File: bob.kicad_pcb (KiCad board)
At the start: 2 copper layers, 58.4 x 25.4 mm, 52 parts, among them J1 Mini USB Female, J2 GPIO (Optional), J3 GPIO (Optional), J4 Screw Terminal, 2.54mm, J5 Conn_01x04_Male, J6 Conn_01x03_Male, Q1 IRFML8244TRPBF, Q2 IRFML8244TRPBF, U1 W25Q64JVSS, U2 AMS1117-3.3, U3 RP2040, U4 QMI8658C, U5 HP203B, U6 QMC5883L, Y1 12MHz

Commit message: Rev 4 issued for production
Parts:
- removed JP1: BOOTSEL, Button_Switch_SMD:SW_SPST_B3U-1000P
- removed TP1, TP2: TestPoint, TestPoint:TestPoint_Pad_D1.0mm
- removed the YAR at (23.4, 30.5)
- added BZ1: Buzzer, YAR_other:Cy-SMD-4020-3040, F.Cu at (50.4, 23.4)
- added C15: 220n, Capacitor_SMD:C_0603_1608Metric, B.Cu at (31.0, 35.1)
- added C16: 100n, Capacitor_SMD:C_0603_1608Metric, B.Cu at (31.0, 36.6)
- added C17: 10u, Capacitor_SMD:C_0603_1608Metric, B.Cu at (26.2, 20.6)
- added C18: 10u, Capacitor_SMD:C_0603_1608Metric, B.Cu at (26.2, 22.1)
- added D6: B5819W SL, Diode_SMD:D_SOD-123, F.Cu at (63.2, 30.0)
- added D7: B5819W SL, Diode_SMD:D_SOD-123, F.Cu at (63.1, 37.8)
- added Q3: AO3400A, Package_TO_SOT_SMD:SOT-23, F.Cu at (63.1, 34.5)
- added R10: 220, Resistor_SMD:R_0603_1608Metric, B.Cu at (37.1, 25.7)
- added R11: 220, Resistor_SMD:R_0603_1608Metric, B.Cu at (37.1, 27.2)
- added R12: 1k, Resistor_SMD:R_0603_1608Metric, B.Cu at (26.2, 41.7)
- added R8: 3k6, Resistor_SMD:R_0603_1608Metric, B.Cu at (46.2, 35.1)
- added R9: 3k6, Resistor_SMD:R_0603_1608Metric, B.Cu at (46.2, 36.6)
- added SW1: Bootsel, Button_Switch_SMD:SW_SPST_TL3342, F.Cu at (23.4, 35.6)
- added U7: W25Q128JVSS, Package_SO:SOIC-8_5.23x5.23mm_P1.27mm, F.Cu at (57.4, 25.7)
- added YAR: LOGO, YAR_Logos:yar_new, B.Cu at (24.1, 27.9)
- C1: value 100n -> 7p; footprint Capacitor_SMD:C_0603_1608Metric -> Capacitor_SMD:C_0402_1005Metric
- C10, C11, C5: moved to B.Cu
- C12: value 4.7u -> 100n; moved to B.Cu
- C13: value 220n -> 100n; moved to B.Cu
- C14: value 100n -> 4.7u; moved to B.Cu
- C2: value 10u -> 7p; footprint Capacitor_SMD:C_0603_1608Metric -> Capacitor_SMD:C_0402_1005Metric
- C3: value 10u -> 100n; moved to B.Cu
- C4, C6: value 1u -> 100n; moved to B.Cu
- C7: value 100n -> 1u; moved to B.Cu
- C8: value 4p -> 1u; moved to B.Cu
- C9: value 4p -> 100n; moved to B.Cu
- D1, D2, D5: value 1N4007 -> B5819W SL
- D3: value RED -> GREEN
- D4: value 1N4007 -> RED; footprint Diode_SMD:D_SOD-123 -> LED_SMD:LED_0603_1608Metric
- J1: value Mini USB Female -> Micro USB Female; footprint Connector_USB:USB_Mini-B_Lumberg_2486_01_Horizontal -> Connector_USB:USB_Micro-B_Molex-105017-0001
- J2: value GPIO (Optional) -> Screw Terminal, 2.54mm; footprint Connector_PinHeader_2.54mm:PinHeader_1x07_P2.54mm_Vertical_NoSilk -> YAR_Connectors:ScrewTerm_2.54x02
- J3: footprint Connector_PinHeader_2.54mm:PinHeader_1x07_P2.54mm_Vertical_NoSilk -> Connector_PinHeader_2.54mm:PinHeader_1x11_P2.54mm_Vertical
- J4: value Screw Terminal, 2.54mm -> GPIO (Optional); footprint YAR_Connectors:ScrewTerm_2.54x06 -> Connector_PinHeader_2.54mm:PinHeader_1x11_P2.54mm_Vertical
- J5: value Conn_01x04_Male -> Conn_01x03_Male; footprint YAR_Connectors:ScrewTerm_2.54x04 -> Connector_PinHeader_2.54mm:PinHeader_1x03_P2.54mm_Vertical
- J6: value Conn_01x03_Male -> Conn_01x06_Pin; footprint Connector_PinHeader_2.54mm:PinHeader_1x02_P2.54mm_Vertical -> YAR_Connectors:ScrewTerm_2.54x06; moved to F.Cu
- Q1, Q2: value IRFML8244TRPBF -> AO3400A
- R1: value 220 -> 27; footprint Resistor_SMD:R_0603_1608Metric -> Resistor_SMD:R_0603_1608Metric_Pad0.98x0.95mm_HandSolder
- R3: value 27 -> 1k; footprint Resistor_SMD:R_0603_1608Metric_Pad0.98x0.95mm_HandSolder -> Resistor_SMD:R_0603_1608Metric
- R4, R5: value 1k -> 3k6
- R6, R7: value 10k -> 4; footprint Resistor_SMD:R_0603_1608Metric -> Resistor_SMD:R_0805_2012Metric; moved to B.Cu
- RN1, RN2: value 22k -> 10k; moved to B.Cu
- U1: value W25Q64JVSS -> AMS1117-3.3; footprint Package_SO:SOIC-8_5.23x5.23mm_P1.27mm -> Package_TO_SOT_SMD:SOT-223-3_TabPin2
- U2: value AMS1117-3.3 -> W25Q128JVSS; footprint Package_TO_SOT_SMD:SOT-223-3_TabPin2 -> Package_SO:SOIC-8_5.23x5.23mm_P1.27mm
- U3: value RP2040 -> QMC5883L; footprint YAR_MCU:RP2040-QFN-56_HS -> YAR_Sensors:QMC5883L-LGA16
- U4: value QMI8658C -> HP203B; footprint YAR_Sensors:QMI8658C-LGA14 -> YAR_Sensors:HP203B-LGA8
- U5: value HP203B -> RP2040; footprint YAR_Sensors:HP203B-LGA8 -> YAR_MCU:RP2040-QFN-56
- U6: value QMC5883L -> QMI8658C; footprint YAR_Sensors:QMC5883L-LGA16 -> YAR_Sensors:QMI8658C-LGA14
- Y1: footprint Crystal:Crystal_SMD_5032-2Pin_5.0x3.2mm -> Crystal:Crystal_SMD_3225-4Pin_3.2x2.5mm
- moved C14 37.7 mm to (31.0, 33.5), turned to 0 degrees
- moved R4 37.6 mm to (66.0, 19.1)
- moved J4 36.2 mm to (30.5, 41.9), turned to 90 degrees
- moved C2 34.8 mm to (54.8, 37.8), turned to 90 degrees
- moved C13 32.2 mm to (37.1, 33.3)
- moved C12 30.7 mm to (40.1, 36.6)
- moved C1 30.6 mm to (49.6, 37.6), turned to -90 degrees
- moved J6 29.5 mm to (69.1, 30.5), turned to 90 degrees
- moved U6 25.3 mm to (43.0, 38.1), turned to -90 degrees
- moved J2 24.7 mm to (17.1, 35.6)
- moved J3 23.4 mm to (30.5, 19.1)
- moved C11 22.9 mm to (40.1, 33.3)
- moved D5 22.4 mm to (60.5, 19.3)
- moved C3 21.9 mm to (56.2, 25.7)
- moved R5 19.3 mm to (66.0, 20.6)
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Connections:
- C1 pad 1: +3V3 -> GND
- C1 pad 2: GND -> Net-(U5-XIN)
- C12 pad 1: GND -> +3V3
- C12 pad 2: Net-(C17-Pad2) -> GND
- C13 pad 1: Net-(C18-Pad1) -> +3V3
- C13 pad 2: Net-(C18-Pad2) -> GND
- C14 pad 1: +3V3 -> GND
- C14 pad 2: GND -> Net-(U3-C1)
- C2 pad 1: Net-(C10-Pad1) -> GND
- C2 pad 2: GND -> Net-(C2-Pad2)
- C8 pad 1: GND -> +1V1
- C8 pad 2: Net-(C13-Pad2) -> GND
- C9 pad 1: GND -> +3V3
- C9 pad 2: XIN -> GND
- D1 pad 1: Net-(C10-Pad1) -> Net-(D1-K)
- D2 pad 1: Net-(C10-Pad1) -> Net-(D1-K)
- D3 pad 1: Net-(D1-Pad1) -> Net-(D3-K)
- D3 pad 2: Net-(D1-Pad2) -> Net-(D3-A)
- D4 pad 1: +3V3 -> Net-(D4-K)
- D4 pad 2: Cont 2 -> +3V3
- D5 pad 2: Cont 1 -> Net-(D5-A)
- F1 pad 1: Net-(F1-Pad1) -> Net-(J6-Pin_5)
- J2 pad 1: VBUS -> GND
- J3 pad 1: +3V3 -> VBUS
- J3 pad 2: GPIO0 -> +BATT
- J3 pad 3: GPIO1 -> GPIO29
- J3 pad 4: GPIO2 -> GPIO28
- J3 pad 5: GPIO3 -> GPIO27
- J3 pad 6: GPIO4 -> GPIO26
- J3 pad 7: GND -> GPIO24
- J4 pad 1: GND -> +3V3
- J4 pad 2: Net-(J2-Pad2) -> GPIO0
- J4 pad 3: Net-(J2-Pad2) -> GPIO1
- J4 pad 4: +BATT -> GPIO2
- J4 pad 5: +BATT -> GPIO3
- J4 pad 6: Net-(F1-Pad1) -> GPIO4
- J5 pad 1: Fire 1 -> GND
- J5 pad 2: ARM -> SWD
- J5 pad 3: Fire 2 -> SWCLK
- J6 pad 1: SWD -> GND
- J6 pad 2: SWCLK -> Cont 2
- Q1 pad 1: Pyro 1 -> BUZZER
- Q1 pad 2: Fire 1 -> GND
- Q1 pad 3: GND -> Net-(BZ1-+)
- Q2 pad 1: Pyro 2 -> Pyro 1
- Q2 pad 2: Fire 2 -> Cont 1
- Q2 pad 3: GND -> Net-(Q2-D)
- R1 pad 1: Net-(D1-Pad1) -> Net-(U5-USB_DM)
- R1 pad 2: GND -> USB_D-
- R2 pad 1: Net-(R2-Pad1) -> Net-(U5-USB_DP)
- R2 pad 2: USB_D- -> USB_D+
- R3 pad 1: Net-(R1-Pad1) -> Net-(C2-Pad2)
- R3 pad 2: USB_D+ -> Net-(U5-XOUT)
- R4 pad 1: Net-(JP1-Pad2) -> ARMED
- R4 pad 2: QSPI_SS -> Net-(D5-A)
- R5 pad 1: Net-(C13-Pad2) -> Net-(D5-A)
- R5 pad 2: XOUT -> ARM
- R6 pad 1: I2C_SCL -> ARM
- R6 pad 2: +3V3 -> Net-(Q2-D)
- R7 pad 1: I2C_SDA -> ARM
- R7 pad 2: +3V3 -> Net-(Q3-D)
- RN1 pad 1: Pyro 2 -> GND
- RN1 pad 2: Fire 2 -> Cont 1
- RN1 pad 3: Cont 2 -> Net-(RN1C-R3.1)
- RN1 pad 4: Net-(RN2-Pad4) -> GND
- RN1 pad 5: GND -> Net-(RN1C-R3.1)
- RN1 pad 6: Net-(RN2-Pad4) -> Cont 1
- RN1 pad 7: Cont 2 -> ARM
- RN1 pad 8: GND -> Pyro 1
- RN2 pad 1: Pyro 1 -> GND
- RN2 pad 2: Fire 1 -> Cont 2
- RN2 pad 3: Cont 1 -> Net-(RN2C-R3.1)
- RN2 pad 4: Net-(RN1-Pad4) -> GND
- RN2 pad 5: GND -> Net-(RN2C-R3.1)
- RN2 pad 6: Net-(RN1-Pad4) -> Cont 2
- RN2 pad 7: Cont 1 -> ARM
- RN2 pad 8: GND -> Pyro 2
- U1 pad 1: QSPI_SS -> GND
- U1 pad 2: QSPI_SD1 -> +3V3
- U1 pad 3: QSPI_SD2 -> Net-(D1-K)
- U2 pad 1: GND -> QSPI_SS
- U2 pad 2: +3V3 -> QSPI_SD1
- U2 pad 3: Net-(C10-Pad1) -> QSPI_SD2
- U3 pad 1: +3V3 -> I2C_SCL
- U3 pad 10: +3V3 -> Net-(U3-C1)
- U3 pad 11: Pyro 2 -> GND
- U3 pad 12: unconnected-(U1-Pad12) -> Net-(U3-SETC)
- U3 pad 13: QMI_INT2 -> +3V3
- U3 pad 14: QMI_INT1 -> (no net)
- U3 pad 15: I2C_SDA -> QMC_DRDY
- U3 pad 16: I2C_SCL -> I2C_SDA
- U3 pad 2: GPIO0 -> +3V3
- U3 pad 3: GPIO1 -> (no net)
- U3 pad 4: GPIO2 -> +3V3
- U3 pad 5: GPIO3 -> (no net)
- U3 pad 6: GPIO4 -> (no net)
- U3 pad 7: Cont 1 -> (no net)
- U3 pad 8: Cont 2 -> Net-(U3-SETP)
- U3 pad 9: Pyro 1 -> GND
- U4 pad 1: GND -> unconnected-(U4-INT1-Pad1)
- U4 pad 3: GND -> +3V3
- U4 pad 4: QMI_INT1 -> (no net)
- U4 pad 5: (no net) -> I2C_SCL
- U4 pad 6: GND -> I2C_SDA
- U4 pad 7: GND -> unconnected-(U4-INT0-Pad7)
- U5 pad 1: unconnected-(U5-Pad1) -> +3V3
- U5 pad 2: GND -> GPIO0
- U5 pad 3: +3V3 -> GPIO1
- U5 pad 4: (no net) -> GPIO2
- U5 pad 5: I2C_SCL -> GPIO3
- U5 pad 6: I2C_SDA -> GPIO4
- U5 pad 7: unconnected-(U5-Pad7) -> GPIO5
- U5 pad 8: +3V3 -> GPIO6
- U6 pad 1: I2C_SCL -> GND
- U6 pad 10: Net-(C17-Pad2) -> (no net)
- U6 pad 11: GND -> (no net)
- U6 pad 12: Net-(C18-Pad2) -> +3V3
- U6 pad 13: +3V3 -> I2C_SCL
- U6 pad 14: (no net) -> I2C_SDA
- U6 pad 2: +3V3 -> GND
- U6 pad 3: (no net) -> GND
- U6 pad 4: +3V3 -> QMI_INT1
- U6 pad 6: (no net) -> GND
- U6 pad 7: (no net) -> GND
- U6 pad 8: Net-(C18-Pad1) -> +3V3
- U6 pad 9: GND -> QMI_INT2
- Y1 pad 1: Net-(C13-Pad2) -> Net-(C2-Pad2)
- Y1 pad 2: XIN -> GND
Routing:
- net +3V3: track 117.1 -> 18.4 mm, vias 10 -> 27
- net ARMED: track 0.00 -> 26.2 mm, vias 0 -> 1
- net Cont 1: track 15.3 -> 39.2 mm, vias 0 -> 3
- net Cont 2: track 12.4 -> 35.9 mm, vias 0 -> 3
- net +BATT: track 48.9 -> 70.9 mm, vias 1 -> 2
- net +1V1: track 20.7 -> 2.02 mm, vias 0 -> 2
- net GPIO6: track 0.00 -> 15.7 mm
- net Net-(F1-Pad1): track 15.0 -> 0.00 mm, vias 1 -> 0
- net SPI_TX: track 0.00 -> 14.5 mm, vias 0 -> 2
- net Fire 2: track 14.1 -> 0.00 mm
- net GPIO5: track 0.00 -> 14.0 mm
- net SPI_SCLK: track 0.00 -> 13.7 mm, vias 0 -> 2
- net SWCLK: track 5.67 -> 19.1 mm
- net SWD: track 7.31 -> 20.6 mm
- net XIN: track 11.6 -> 0.00 mm
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- added copper zone on F.Cu, net +1V1
- added copper zone on In1.Cu, net +3V3
- added copper zone on In2.Cu, net GND
- removed copper zone on F.Cu, net +BATT
- removed copper zone on F.Cu, net Net-(C10-Pad1)
- removed copper zone on B.Cu, net Net-(J2-Pad2)
- removed copper zone on F.Cu, net Net-(J2-Pad2)
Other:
- copper layers 2 -> 4
- board text added: "00"
- board text added: "01"
- board text added: "02"
- board text added: "03"
- board text added: "04"
- board text added: "05"
- board text added: "06"
- board text added: "12V MAX"
- board text added: "22"
- board text added: "23"
- board text added: "24"
- board text added: "3v3"
- board text added: "ARMED"
- board text added: "Bob Rev 4A Claire H 2023"
- board text added: "DRG"
- board text added: "MAIN"
- board text added: "POWER"
- board text added: "STATUS"
- board text added: "VBAT"
- board text added: "VBUS"
- board text removed: "+ -"
- board text removed: "0"
- board text removed: "1"
- board text removed: "2"
- board text removed: "3"
- board text removed: "3V3"
- board text removed: "4"
- board text removed: "BAT"
- board text removed: "BUS"
- board text removed: "Bob Rev 4"
- board text removed: "PYRO 1"
- board text removed: "PYRO 2"
- board text removed: "SWITCH"
- board text removed: "Sensitive Crystal Do not route underneath"
- board text removed: "USB Requires GND underneath"
- board text removed: "X"
- board text removed: "Y"
- board text removed: "Z"

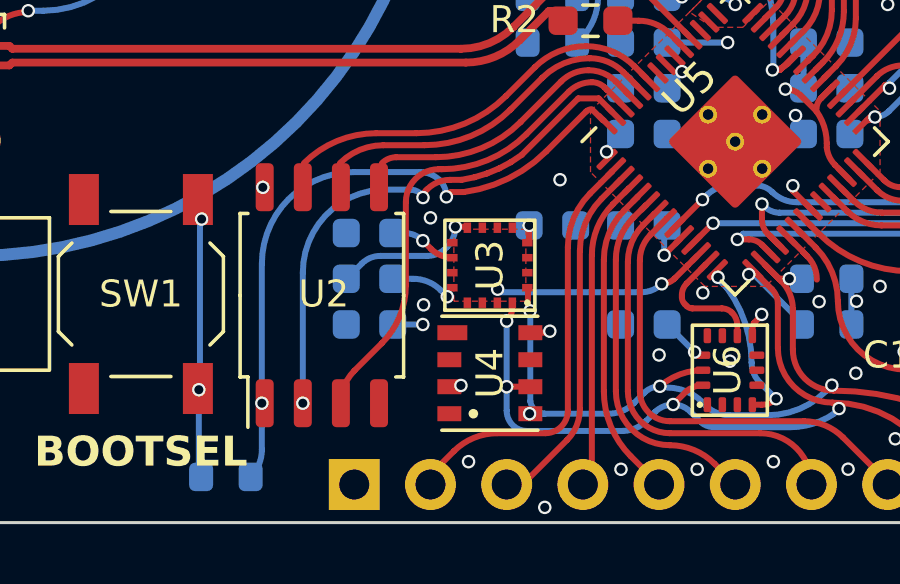
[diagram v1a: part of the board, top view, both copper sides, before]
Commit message: Moved via from HP203 SCK pad
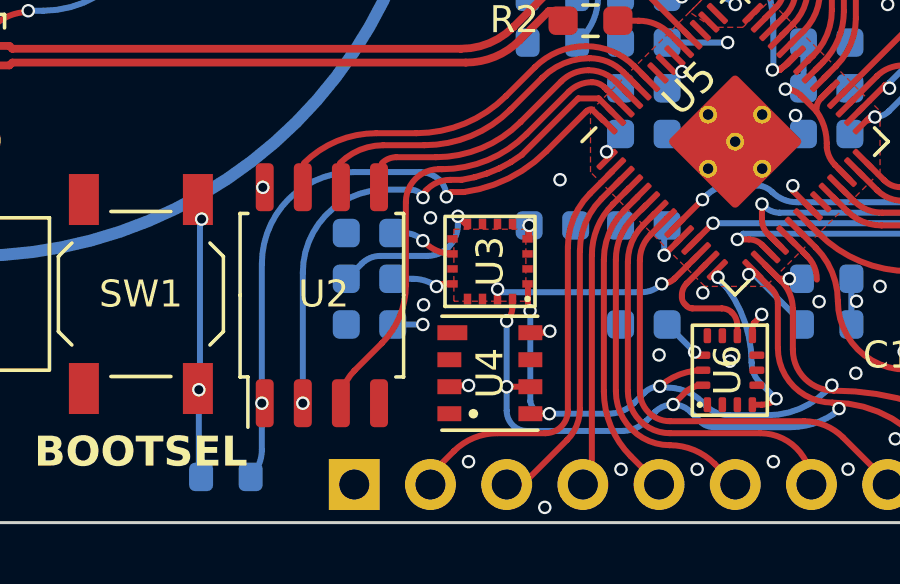
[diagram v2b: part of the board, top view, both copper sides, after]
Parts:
- moved U3 0.13 mm to (35.0, 34.5)
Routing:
- net +3V3: track 18.4 -> 18.9 mm
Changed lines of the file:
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@@
   )
   (footprint "YAR_Sensors:QMC5883L-LGA16" (layer "F.Cu")
-    (at 35 34.6 90)
+    (at 35.0052 34.4732 90)
     (descr "16-PIN LGA PACKAGE")
     (tags "16-PIN LGA PACKAGE")
@@
   (segment (start 45.862944 32.884163) (end 45.1 32.121219) (width 0.2) (layer "F.Cu") (net 2))
   (segment (start 45.456225 29.033775) (end 45.880662 29.458212) (width 0.2) (layer "F.Cu") (net 2))
+  (segment (start 33.692 38.608) (end 33.65 38.65) (width 0.2) (layer "F.Cu") (net 2))
   (segment (start 36.309 33.274) (end 36.309 33.707562) (width 0.2) (layer "F.Cu") (net 2))
   (segment (start 36.35 36.85) (end 36.87879 36.85) (width 0.2) (layer "F.Cu") (net 2))
@@
   (segment (start 40.809567 34.267892) (end 40.809567 34.260584) (width 0.2) (layer "F.Cu") (net 2))
   (segment (start 46.229874 30.532259) (end 46.229874 30.681534) (width 0.2) (layer "F.Cu") (net 2))
+  (segment (start 34.29 38.608) (end 33.692 38.608) (width 0.2) (layer "F.Cu") (net 2))
   (segment (start 46.506955 31.261371) (end 46.998377 31.752792) (width 0.2) (layer "F.Cu") (net 2))
   (segment (start 45.366315 28.943864) (end 45.456225 29.033775) (width 0.2) (layer "F.Cu") (net 2))
@@
   (via (at 39.116 23.368) (size 0.45) (drill 0.3) (layers "F.Cu" "B.Cu") (net 2))
   (via (at 58.674 19.304) (size 0.45) (drill 0.3) (layers "F.Cu" "B.Cu") (net 2))
-  (via (at 34.036 38.608) (size 0.45) (drill 0.3) (layers "F.Cu" "B.Cu") (net 2))
+  (via (at 34.29 38.608) (size 0.45) (drill 0.3) (layers "F.Cu" "B.Cu") (net 2))
   (via (at 43.18 25.908) (size 0.45) (drill 0.3) (layers "F.Cu" "B.Cu") (free) (net 2))
   (via (at 32.766 36.576) (size 0.45) (drill 0.3) (layers "F.Cu" "B.Cu") (net 2))
@@
   (arc (start 46.229874 30.681534) (mid 46.319436 30.995124) (end 46.506955 31.261371) (width 0.2) (layer "F.Cu") (net 2))
   (arc (start 44.85 28.73) (mid 45.129427 28.785582) (end 45.366315 28.943864) (width 0.2) (layer "F.Cu") (net 2))
-  (arc (start 36.309 33.707562) (mid 36.293666 33.784649) (end 36.25 33.85) (width 0.2) (layer "F.Cu") (net 2))
   (arc (start 46.428629 28.641522) (mid 46.427882 28.645275) (end 46.425757 28.648457) (width 0.2) (layer "F.Cu") (net 2))
   (arc (start 45.862944 32.884163) (mid 45.86272 32.883037) (end 45.862082 32.882082) (width 0.2) (layer "F.Cu") (net 2))
@@
   (segment (start 35.56 38.65) (end 36.35 38.65) (width 0.2) (layer "F.Cu") (net 13))
   (segment (start 44.6 35.882842) (end 44.6 37.359652) (width 0.2) (layer "F.Cu") (net 13))
+  (segment (start 35.75 36.0013) (end 35.75 35.735753) (width 0.2) (layer "F.Cu") (net 13))
   (via (at 35.56 36.46) (size 0.45) (drill 0.3) (layers "F.Cu" "B.Cu") (net 13))
   (via (at 46.637428 39.377428) (size 0.45) (drill 0.3) (layers "F.Cu" "B.Cu") (net 13))
@@
   (arc (start 43.883045 34.864062) (mid 43.886534 34.8816) (end 43.896468 34.896468) (width 0.2) (layer "F.Cu") (net 13))
   (arc (start 44.4 35.4) (mid 44.548021 35.62153) (end 44.6 35.882842) (width 0.2) (layer "F.Cu") (net 13))
+  (arc (start 35.75 35.735753) (mid 35.751351 35.72896) (end 35.7552 35.7232) (width 0.2) (layer "F.Cu") (net 13))
   (arc (start 44.6 37.359652) (mid 45.133168 38.646832) (end 46.420347 39.18) (width 0.2) (layer "F.Cu") (net 13))
   (segment (start 35.561557 36.323557) (end 35.56 36.322) (width 0.2) (layer "B.Cu") (net 13))
@@
   (segment (start 40.623139 38.68) (end 40.665771 38.637368) (width 0.2) (layer "F.Cu") (net 14))
   (segment (start 44.633989 35.049321) (end 44.165887 34.581219) (width 0.2) (layer "F.Cu") (net 14))
+  (segment (start 36.35 39.55) (end 36.9824 39.55) (width 0.2) (layer "F.Cu") (net 14))
   (segment (start 36.34 36.12) (end 36.27 36.05) (width 0.2) (layer "F.Cu") (net 14))
-  (via (at 36.325 39.55) (size 0.45) (drill 0.3) (layers "F.Cu" "B.Cu") (net 14))
+  (via (at 36.9824 39.55) (size 0.45) (drill 0.3) (layers "F.Cu" "B.Cu") (net 14))
   (via (at 40.665771 38.637368) (size 0.45) (drill 0.3) (layers "F.Cu" "B.Cu") (net 14))
   (via (at 46.4 38.6) (size 0.45) (drill 0.3) (layers "F.Cu" "B.Cu") (net 14))
@@
   (segment (start 36.825 39.55) (end 38.955026 39.55) (width 0.2) (layer "B.Cu") (net 14))
   (segment (start 44.982724 35.049321) (end 45.258535 35.049321) (width 0.2) (layer "B.Cu") (net 14))
+  (segment (start 36.825 39.55) (end 36.9824 39.55) (width 0.2) (layer "B.Cu") (net 14))
   (segment (start 46.2 38.8) (end 46.4 38.6) (width 0.2) (layer "B.Cu") (net 14))
   (segment (start 36.34 36.12) (end 36.348023 36.128023) (width 0.2) (layer "B.Cu") (net 14))
@@
   (segment (start 39.8 39.2) (end 40.14828 38.85172) (width 0.2) (layer "B.Cu") (net 14))
   (segment (start 42.965685 39.6) (end 44.26863 39.6) (width 0.2) (layer "B.Cu") (net 14))
-  (segment (start 36.825 39.55) (end 36.325 39.55) (width 0.2) (layer "B.Cu") (net 14))
   (arc (start 42.204852 39.284852) (mid 42.553924 39.518096) (end 42.965685 39.6) (width 0.2) (layer "B.Cu") (net 14))
   (arc (start 44.26863 39.6) (mid 45.31388 39.392086) (end 46.2 38.8) (width 0.2) (layer "B.Cu") (net 14))
@@
   (arc (start 48.88 38.08) (mid 47.267797 37.412203) (end 46.6 35.8) (width 0.2) (layer "F.Cu") (net 29))
   (arc (start 46.6 35.8) (mid 46.40677 34.828567) (end 45.856497 34.005025) (width 0.2) (layer "F.Cu") (net 29))
-  (segment (start 33.039843 34.055844) (end 32.766 33.782) (width 0.2) (layer "F.Cu") (net 30))
+  (segment (start 32.766 33.782) (end 32.819705 33.835705) (width 0.2) (layer "F.Cu") (net 30))
   (via (at 32.766 33.782) (size 0.45) (drill 0.3) (layers "F.Cu" "B.Cu") (net 30))
-  (arc (start 33.75 34.35) (mid 33.365666 34.273551) (end 33.039843 34.055844) (width 0.2) (layer "F.Cu") (net 30))
+  (arc (start 32.819705 33.835705) (mid 33.248913 34.122493) (end 33.7552 34.2232) (width 0.2) (layer "F.Cu") (net 30))
   (segment (start 31.763 33.528) (end 32.15279 33.528) (width 0.2) (layer "B.Cu") (net 30))
   (arc (start 32.766 33.782) (mid 32.484657 33.594012) (end 32.15279 33.528) (width 0.2) (layer "B.Cu") (net 30))
-  (segment (start 33.85 33.32) (end 34.177574 33.32) (width 0.2) (layer "F.Cu") (net 31))
-  (via (at 33.85 33.32) (size 0.45) (drill 0.3) (layers "F.Cu" "B.Cu") (net 31))
-  (arc (start 34.177574 33.32) (mid 34.21677 33.327797) (end 34.25 33.35) (width 0.2) (layer "F.Cu") (net 31))
-  (segment (start 33.573095 33.988508) (end 33.466524 34.095079) (width 0.2) (layer "B.Cu") (net 31))
-  (segment (start 32.91479 34.29) (end 31.34721 34.29) (width 0.2) (layer "B.Cu") (net 31))
-  (segment (start 30.734 34.544) (end 30.235193 35.042807) (width 0.2) (layer "B.Cu") (net 31))
-  (arc (start 31.34721 34.29) (mid 31.015343 34.356012) (end 30.734 34.544) (width 0.2) (layer "B.Cu") (net 31))
-  (arc (start 33.85 33.32) (mid 33.778035 33.681794) (end 33.573095 33.988508) (width 0.2) (layer "B.Cu") (net 31))
-  (arc (start 33.466524 34.095079) (mid 33.206946 34.239309) (end 32.91479 34.29) (width 0.2) (layer "B.Cu") (net 31))
-  (via (at 33.58 35.65) (size 0.45) (drill 0.3) (layers "F.Cu" "B.Cu") (net 32))
+  (segment (start 34.141166 33.175965) (end 33.9344 32.9692) (width 0.2) (layer "F.Cu") (net 31))
+  (segment (start 34.1884 33.2232) (end 34.2552 33.2232) (width 0.2) (layer "F.Cu") (net 31))
+  (via (at 33.9344 32.9692) (size 0.45) (drill 0.3) (layers "F.Cu" "B.Cu") (net 31))
+  (arc (start 34.2552 33.2232) (mid 34.193485 33.210924) (end 34.141166 33.175965) (width 0.2) (layer "F.Cu") (net 31))
+  (segment (start 30.235193 35.042807) (end 30.734 34.544) (width 0.2) (layer "B.Cu") (net 31))
+  (segment (start 33.9344 33.249348) (end 33.9344 32.9692) (width 0.2) (layer "B.Cu") (net 31))
+  (segment (start 33.614721 34.000079) (end 33.6296 33.9852) (width 0.2) (layer "B.Cu") (net 31))
+  (segment (start 31.34721 34.29) (end 32.91479 34.29) (width 0.2) (layer "B.Cu") (net 31))
+  (arc (start 30.734 34.544) (mid 31.015343 34.356012) (end 31.34721 34.29) (width 0.2) (layer "B.Cu") (net 31))
+  (arc (start 33.6296 33.9852) (mid 33.855185 33.647589) (end 33.9344 33.249348) (width 0.2) (layer "B.Cu") (net 31))
+  (arc (start 32.91479 34.29) (mid 33.29359 34.214652) (end 33.614721 34.000079) (width 0.2) (layer "B.Cu") (net 31))
+  (segment (start 33.426488 35.2232) (end 33.7552 35.2232) (width 0.2) (layer "F.Cu") (net 32))
+  (segment (start 33.317278 35.404874) (end 33.220802 35.308398) (width 0.2) (layer "F.Cu") (net 32))
+  (via (at 33.220802 35.308398) (size 0.45) (drill 0.3) (layers "F.Cu" "B.Cu") (net 32))
+  (arc (start 33.220802 35.308398) (mid 33.315171 35.245343) (end 33.426488 35.2232) (width 0.2) (layer "F.Cu") (net 32))
+  (segment (start 33.220802 35.308398) (end 33.218629 35.308398) (width 0.2) (layer "B.Cu") (net 32))
+  (segment (start 33.218629 35.308398) (end 33.201245 35.291014) (width 0.2) (layer "B.Cu") (net 32))
   (segment (start 32.44 35.052) (end 31.763 35.052) (width 0.2) (layer "B.Cu") (net 32))
-  (segment (start 33.365252 35.435252) (end 33.58 35.65) (width 0.2) (layer "B.Cu") (net 32))
-  (arc (start 32.44 35.052) (mid 32.940743 35.151604) (end 33.365252 35.435252) (width 0.2) (layer "B.Cu") (net 32))
+  (arc (start 33.201245 35.291014) (mid 32.838369 35.114263) (end 32.44 35.052) (width 0.2) (layer "B.Cu") (net 32))
   (segment (start 43.25 36.614558) (end 43.25 36.65) (width 0.2) (layer "F.Cu") (net 33))
   (segment (start 41.498995 35.898995) (end 41.56 35.96) (width 0.2) (layer "F.Cu") (net 33))
